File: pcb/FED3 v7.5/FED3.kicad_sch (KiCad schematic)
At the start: 32 parts, among them IC2 TB6612FNG, J6 USB4105-GF-A, SW1 Sw, U2 MIC5504-3.3, U3 MCP73834-xxxx, X5 B2B-PH-K-S

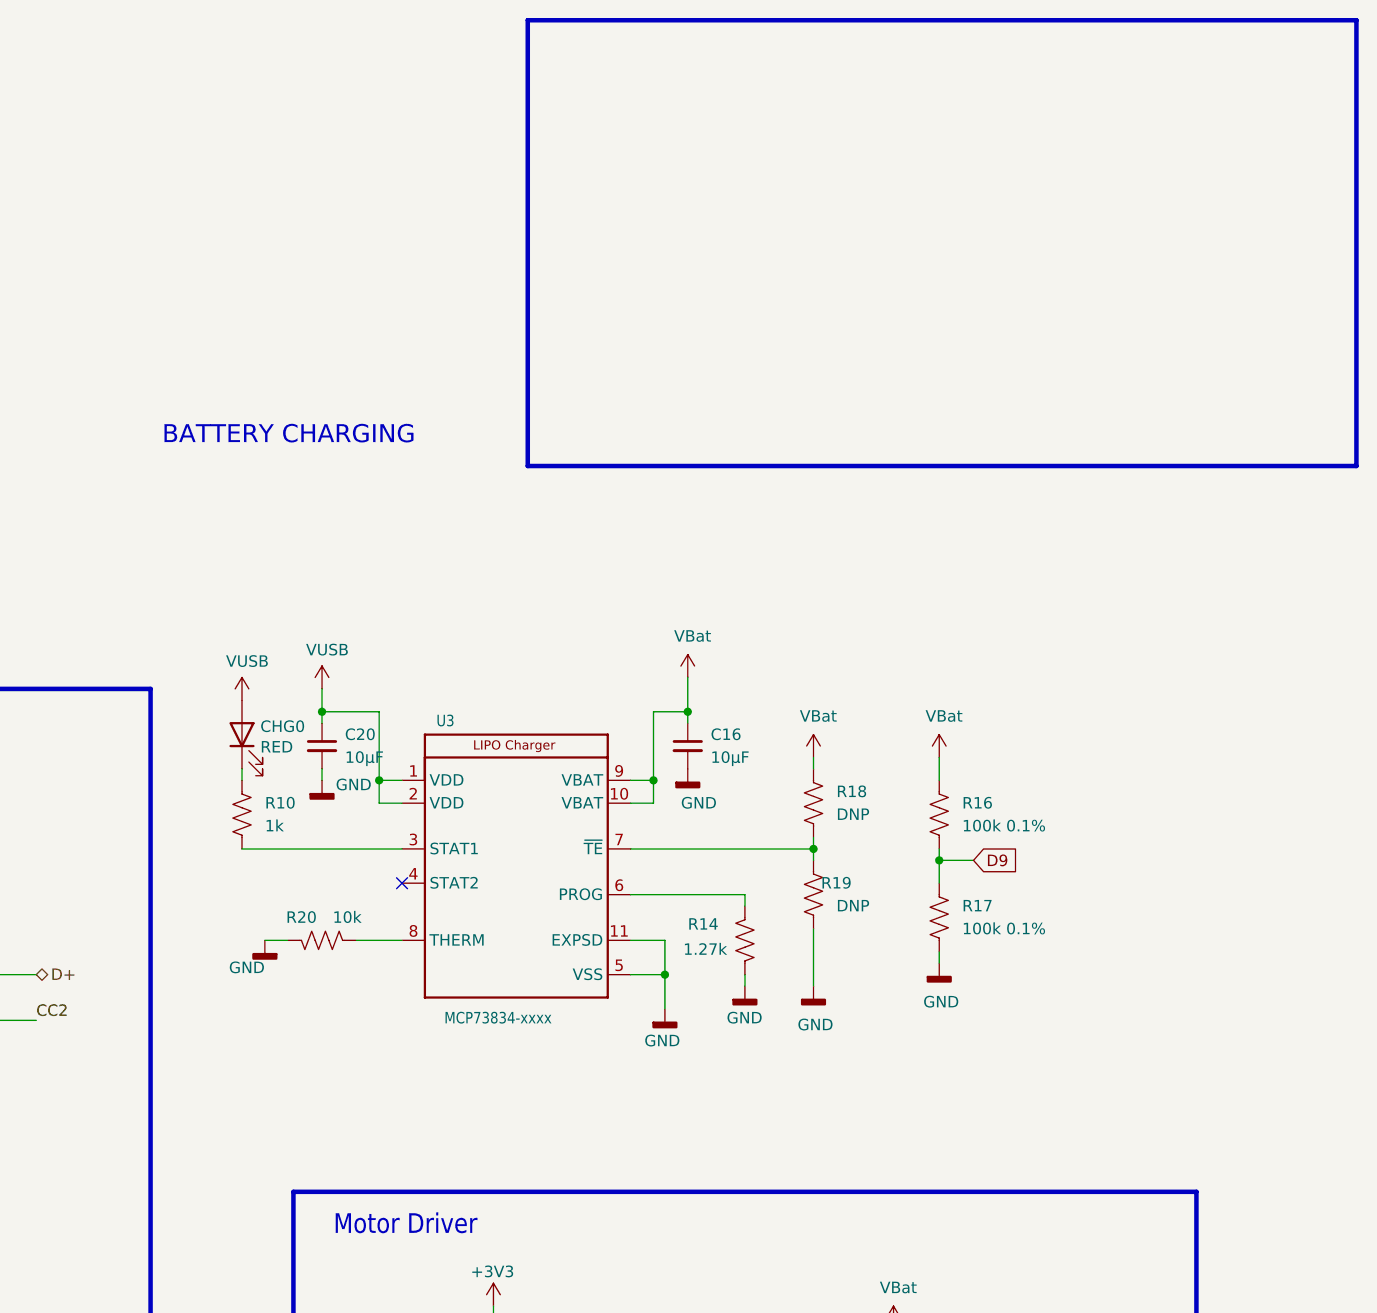
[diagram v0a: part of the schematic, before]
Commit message: FED3 v.7.5 - 1ºs ficheiros de progução
- adicionada header para opção VTherm = Vbat
- optimização para BOM: variedade-vs-quantidade
- optimização de power-planes
- gerados ficheiros produção para 1ª avaliação; há lá erros reconhecidos
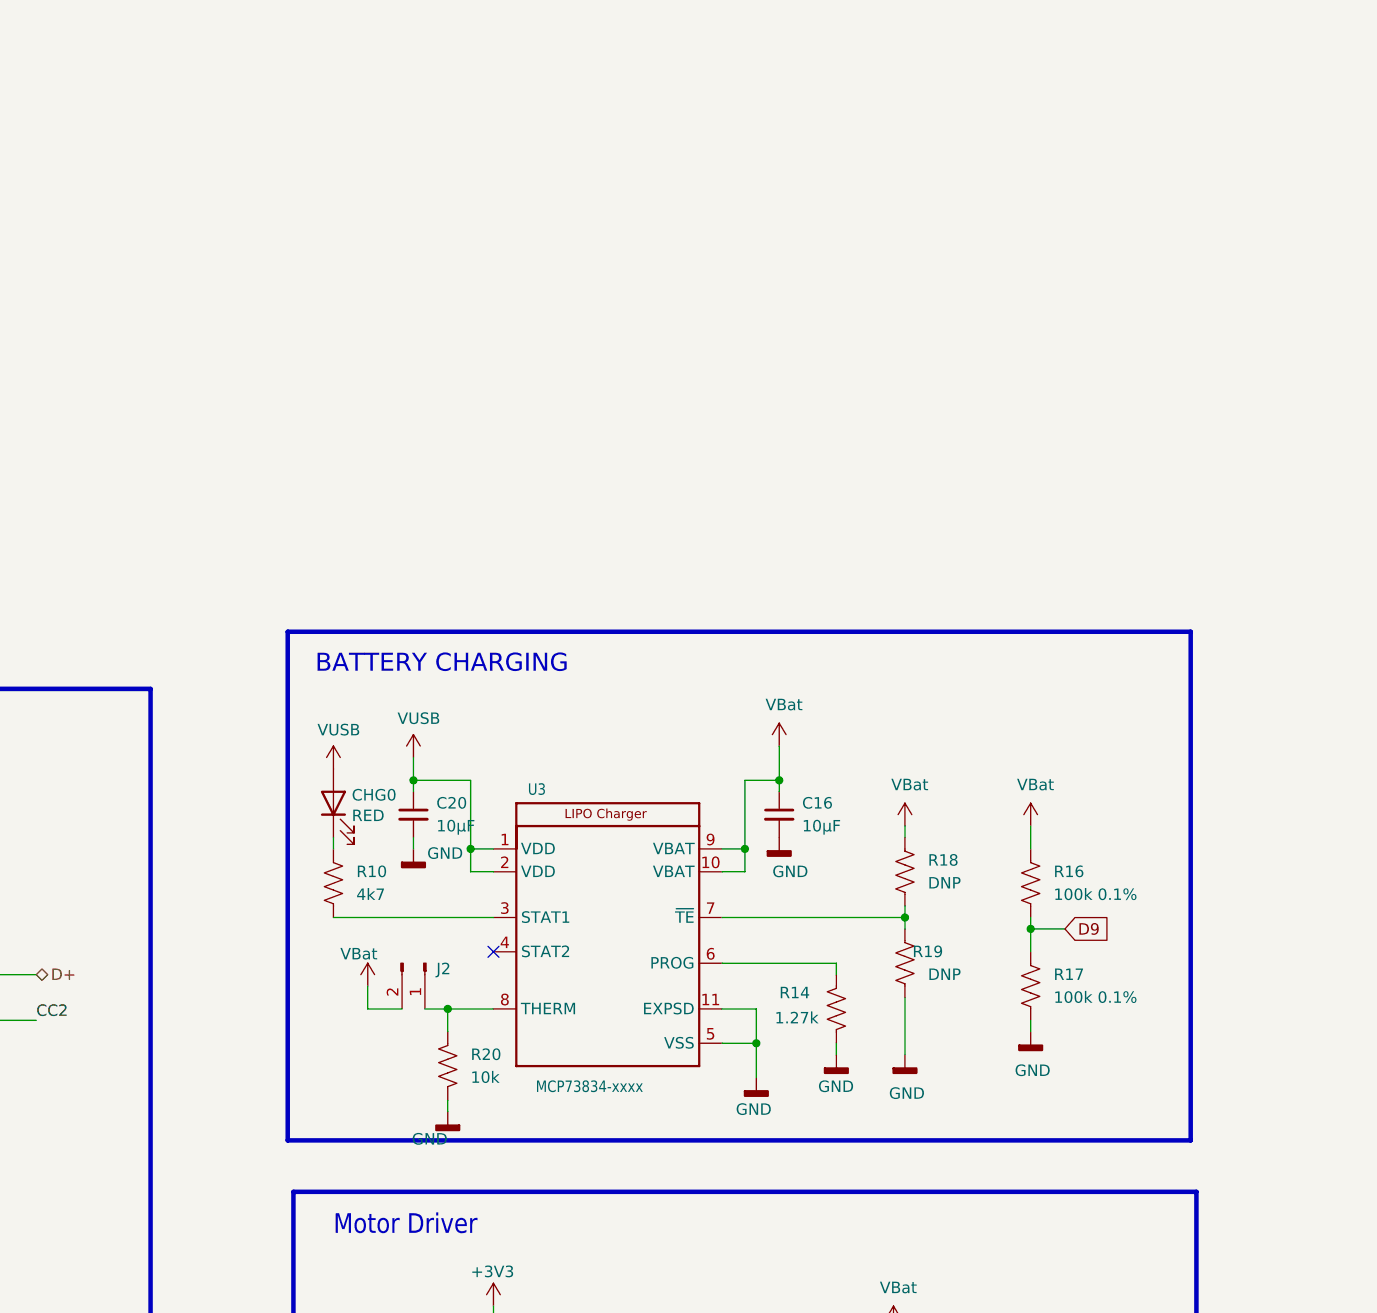
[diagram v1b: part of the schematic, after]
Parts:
- added J2: Conn_01x02_Odd_Even, Connector_PinHeader_2.54mm:PinHeader_1x02_P2.54mm_Vertical, symbol Connector:Conn_01x02_Pin
- R10: value 1k -> 4k7; MPN ERJ-2RKF1001X -> ERJ-2RKF4701X; OEPSPN OEPS020006 -> OEPS020010
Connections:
- net VBat: now also J2.2 (Pin_2)
- net at R20.1, U3.8 (THERM): now also J2.1 (Pin_1)
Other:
- moved on the sheet: C16, C20, CHG0, R10, R14, R16, R17, R18, R19, R20, U3

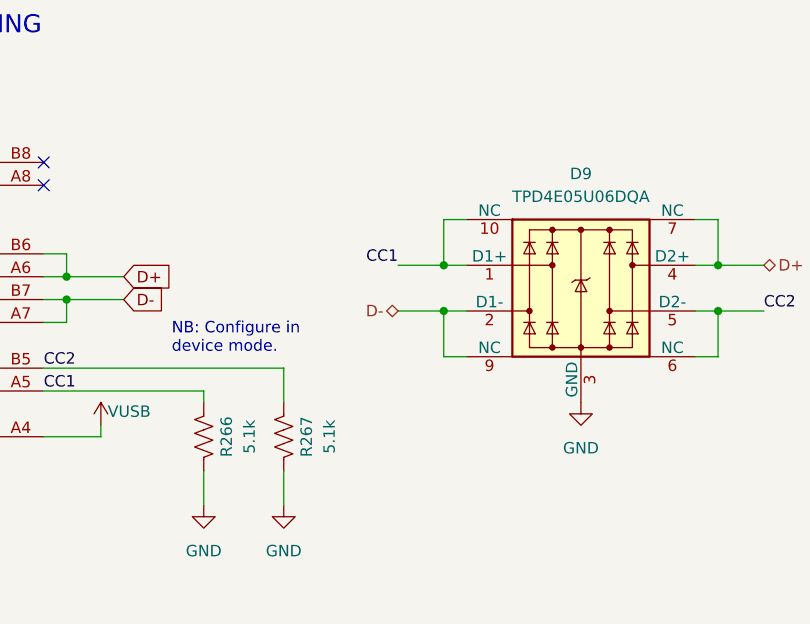
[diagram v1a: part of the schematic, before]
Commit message: FED3 v.7.5 - 2ºs ficheiros produção
- corrigidas posições de silks de alguns componentes
- modificados Denominators de alguns componentes
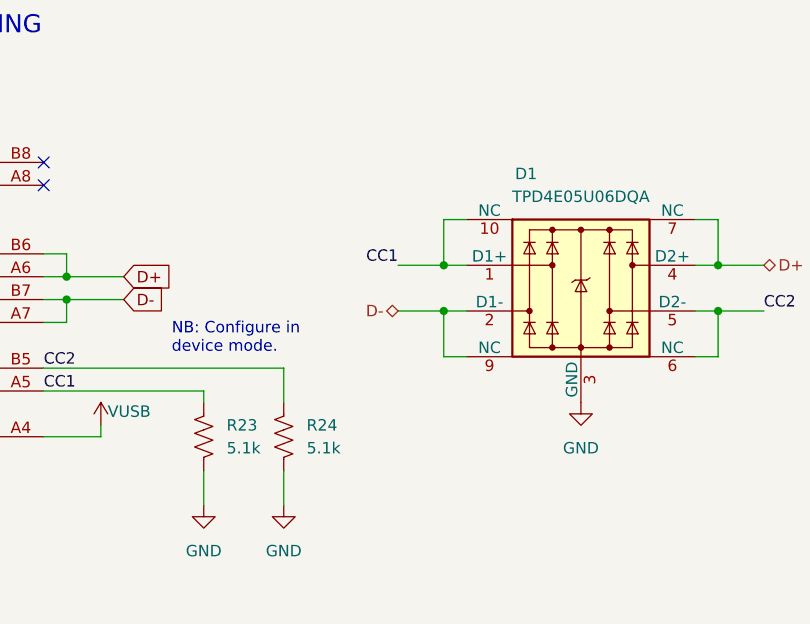
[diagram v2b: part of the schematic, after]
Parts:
- renumbered D9 to D1, R266 to R23, R267 to R24
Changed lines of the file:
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@@
 		(on_board yes)
 		(dnp no)
-		(fields_autoplaced yes)
-		(property "Reference" "D9"
-			(at 121.92 41.91 0)
+		(property "Reference" "D1"
+			(at 115.824 41.91 0)
 			(effects
 				(font
@@
 			(project "FED3"
 				(path "/2ba63f12-2fcd-4471-9636-2762cde37de8"
-					(reference "D9")
+					(reference "D1")
 					(unit 1)
 				)
@@
 		(on_board yes)
 		(dnp no)
-		(property "Reference" "R267"
-			(at 91.44 71.12 90)
-			(effects
-				(font
-					(size 1.27 1.27)
-				)
+		(fields_autoplaced yes)
+		(property "Reference" "R24"
+			(at 91.44 69.8499 0)
+			(effects
+				(font
+					(size 1.27 1.27)
+				)
+				(justify right)
 			)
 		)
 		(property "Value" "5.1k"
-			(at 93.98 71.12 90)
-			(effects
-				(font
-					(size 1.27 1.27)
-				)
+			(at 91.44 72.3899 0)
+			(effects
+				(font
+					(size 1.27 1.27)
+				)
+				(justify right)
 			)
 		)
@@
 			(project "FED3"
 				(path "/2ba63f12-2fcd-4471-9636-2762cde37de8"
-					(reference "R267")
+					(reference "R24")
 					(unit 1)
 				)
@@
 		(on_board yes)
 		(dnp no)
-		(property "Reference" "R266"
-			(at 82.55 71.12 90)
-			(effects
-				(font
-					(size 1.27 1.27)
-				)
+		(fields_autoplaced yes)
+		(property "Reference" "R23"
+			(at 82.55 69.8499 0)
+			(effects
+				(font
+					(size 1.27 1.27)
+				)
+				(justify right)
 			)
 		)
 		(property "Value" "5.1k"
-			(at 85.09 71.12 90)
-			(effects
-				(font
-					(size 1.27 1.27)
-				)
+			(at 82.55 72.3899 0)
+			(effects
+				(font
+					(size 1.27 1.27)
+				)
+				(justify right)
 			)
 		)
@@
 			(project "FED3"
 				(path "/2ba63f12-2fcd-4471-9636-2762cde37de8"
-					(reference "R266")
-					(unit 1)
-				)
+					(reference "R23")
+					(unit 1)
+				)
